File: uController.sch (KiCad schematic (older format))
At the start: 37 parts, among them J4 USB_C_Receptacle, U13 STM32F446RETx, U14 STM14_SW, Y1 16Mhz, 18pF

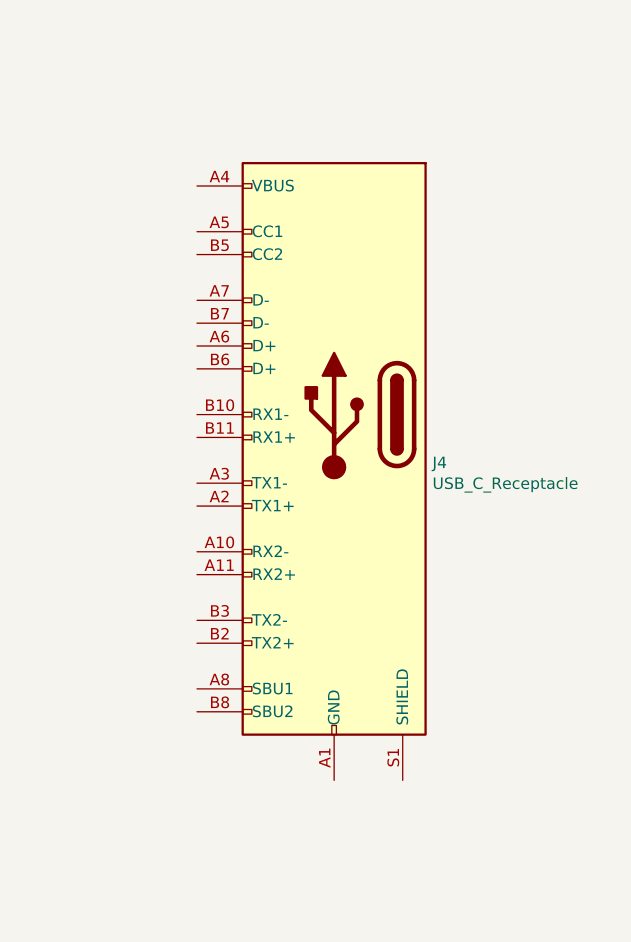
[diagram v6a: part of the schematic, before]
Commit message: USB-C PD charging and cell balancing.
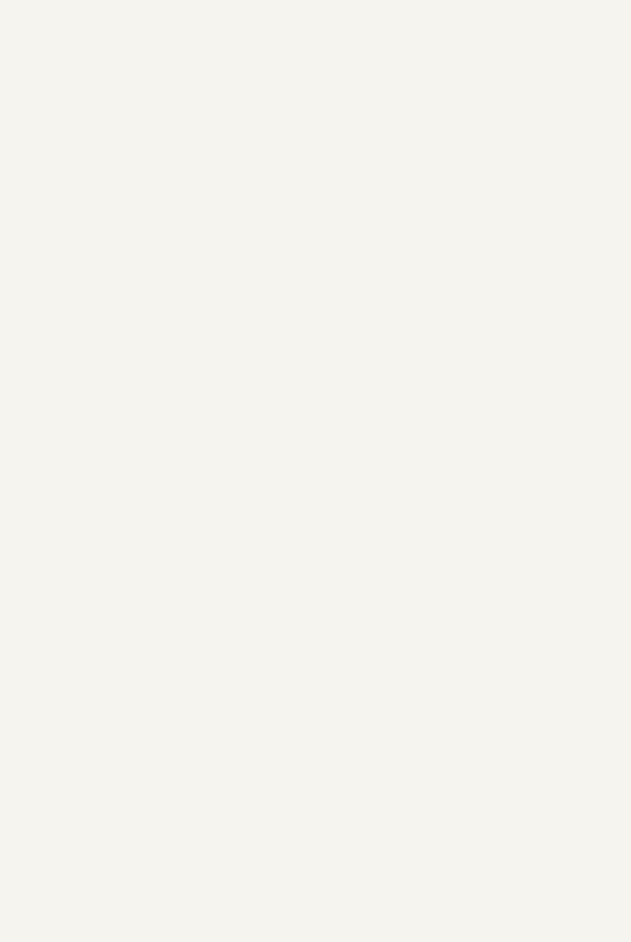
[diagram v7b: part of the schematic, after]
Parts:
- removed J4: USB_C_Receptacle, Connector_USB:USB_C_Receptacle_GCT_USB4085, symbol synermycha-electronics-rescue:USB_C_Receptacle-Connector
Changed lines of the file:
@@
 Connection ~ 3600 5750
-$Comp
-L Device:R_Small R42
-U 1 1 5E839F84
-P 2700 3550
-F 0 "R42" H 2759 3596 50  0000 L CNN
-F 1 "140R" H 2759 3505 50  0000 L CNN
-F 2 "Resistor_SMD:R_0402_1005Metric" H 2700 3550 50  0001 C CNN
-F 3 "~" H 2700 3550 50  0001 C CNN
-	1    2700 3550
-	1    0    0    1
-$EndComp
 $Comp
 L Device:R_Small R43
@@
 F 3 "~" H 3600 5850 50  0001 C CNN
 	1    3600 5850
-	-1   0    0    1
-$EndComp
-$Comp
-L Device:LED_Small D16
-U 1 1 5E8A288C
-P 2700 3750
-F 0 "D16" V 2750 3550 50  0000 L CNN
-F 1 "YELLOW" V 2650 3400 50  0000 L CNN
-F 2 "LED_SMD:LED_0402_1005Metric" V 2700 3750 50  0001 C CNN
-F 3 "~" V 2700 3750 50  0001 C CNN
-	1    2700 3750
-	0    -1   -1   0
-$EndComp
-$Comp
-L Device:R_Small R50
-U 1 1 5E8A7FAC
-P 2400 5650
-F 0 "R50" H 2341 5604 50  0000 R CNN
-F 1 "140R" H 2341 5695 50  0000 R CNN
-F 2 "Resistor_SMD:R_0402_1005Metric" H 2400 5650 50  0001 C CNN
-F 3 "~" H 2400 5650 50  0001 C CNN
-	1    2400 5650
 	-1   0    0    1
 $EndComp
@@
 Connection ~ 7150 4650
 $Comp
+L power:+3V3 #PWR0137
+U 1 1 5F64C720
+P 4000 5550
+F 0 "#PWR0137" H 4000 5400 50  0001 C CNN
+F 1 "+3V3" H 4015 5723 50  0000 C CNN
+F 2 "" H 4000 5550 50  0001 C CNN
+F 3 "" H 4000 5550 50  0001 C CNN
+	1    4000 5550
+	1    0    0    -1
+$EndComp
+$Comp
+L power:+3V3 #PWR0140
+U 1 1 5F64D886
+P 3100 3250
+F 0 "#PWR0140" H 3100 3100 50  0001 C CNN
+F 1 "+3V3" H 3115 3423 50  0000 C CNN
+F 2 "" H 3100 3250 50  0001 C CNN
+F 3 "" H 3100 3250 50  0001 C CNN
+	1    3100 3250
+	1    0    0    -1
+$EndComp
+$Comp
+L power:+3V3 #PWR0141
+U 1 1 5F64E077
+P 3100 3900
+F 0 "#PWR0141" H 3100 3750 50  0001 C CNN
+F 1 "+3V3" H 3115 4073 50  0000 C CNN
+F 2 "" H 3100 3900 50  0001 C CNN
+F 3 "" H 3100 3900 50  0001 C CNN
+	1    3100 3900
+	1    0    0    -1
+$EndComp
+$Comp
+L power:+3V3 #PWR0142
+U 1 1 5F657B9E
+P 7300 1650
+F 0 "#PWR0142" H 7300 1500 50  0001 C CNN
+F 1 "+3V3" H 7315 1823 50  0000 C CNN
+F 2 "" H 7300 1650 50  0001 C CNN
+F 3 "" H 7300 1650 50  0001 C CNN
+	1    7300 1650
+	1    0    0    -1
+$EndComp
+Wire Wire Line
+	2650 4100 2700 4100
+Connection ~ 2700 4100
+Wire Wire Line
+	2700 4100 3100 4100
+Wire Wire Line
+	2650 3450 2700 3450
+Connection ~ 2700 3450
+Wire Wire Line
+	2700 3450 3100 3450
+$Comp
+L power:GND #PWR0139
+U 1 1 5F7F8216
+P 7850 2250
+F 0 "#PWR0139" H 7850 2000 50  0001 C CNN
+F 1 "GND" H 7855 2077 50  0000 C CNN
+F 2 "" H 7850 2250 50  0001 C CNN
+F 3 "" H 7850 2250 50  0001 C CNN
+	1    7850 2250
+	1    0    0    -1
+$EndComp
+$Comp
+L power:GND #PWR0143
+U 1 1 5F7FF6EF
+P 3600 6150
+F 0 "#PWR0143" H 3600 5900 50  0001 C CNN
+F 1 "GND" H 3605 5977 50  0000 C CNN
+F 2 "" H 3600 6150 50  0001 C CNN
+F 3 "" H 3600 6150 50  0001 C CNN
+	1    3600 6150
+	1    0    0    -1
+$EndComp
+$Comp
+L power:GND #PWR0135
+U 1 1 5F7F5F84
+P 2400 5950
+F 0 "#PWR0135" H 2400 5700 50  0001 C CNN
+F 1 "GND" H 2405 5777 50  0000 C CNN
+F 2 "" H 2400 5950 50  0001 C CNN
+F 3 "" H 2400 5950 50  0001 C CNN
+	1    2400 5950
+	1    0    0    -1
+$EndComp
+$Comp
+L power:GND #PWR0136
+U 1 1 5F7F697D
+P 2700 4500
+F 0 "#PWR0136" H 2700 4250 50  0001 C CNN
+F 1 "GND" H 2705 4327 50  0000 C CNN
+F 2 "" H 2700 4500 50  0001 C CNN
+F 3 "" H 2700 4500 50  0001 C CNN
+	1    2700 4500
+	1    0    0    -1
+$EndComp
+$Comp
+L power:GND #PWR0138
+U 1 1 5F7F738B
+P 2700 3850
+F 0 "#PWR0138" H 2700 3600 50  0001 C CNN
+F 1 "GND" H 2705 3677 50  0000 C CNN
+F 2 "" H 2700 3850 50  0001 C CNN
+F 3 "" H 2700 3850 50  0001 C CNN
+	1    2700 3850
+	1    0    0    -1
+$EndComp
+$Comp
+L Device:R_Small R42
+U 1 1 5E839F84
+P 2700 3550
+F 0 "R42" H 2759 3596 50  0000 L CNN
+F 1 "140R" H 2759 3505 50  0000 L CNN
+F 2 "Resistor_SMD:R_0402_1005Metric" H 2700 3550 50  0001 C CNN
+F 3 "~" H 2700 3550 50  0001 C CNN
+	1    2700 3550
+	1    0    0    1
+$EndComp
+$Comp
+L Device:LED_Small D16
+U 1 1 5E8A288C
+P 2700 3750
+F 0 "D16" V 2750 3550 50  0000 L CNN
+F 1 "YELLOW" V 2650 3400 50  0000 L CNN
+F 2 "LED_SMD:LED_0402_1005Metric" V 2700 3750 50  0001 C CNN
+F 3 "~" V 2700 3750 50  0001 C CNN
+	1    2700 3750
+	0    -1   -1   0
+$EndComp
+$Comp
 L power:+3V3 #PWR0134
 U 1 1 5F64A100
@@
 $EndComp
 $Comp
-L power:+3V3 #PWR0137
-U 1 1 5F64C720
-P 4000 5550
-F 0 "#PWR0137" H 4000 5400 50  0001 C CNN
-F 1 "+3V3" H 4015 5723 50  0000 C CNN
-F 2 "" H 4000 5550 50  0001 C CNN
-F 3 "" H 4000 5550 50  0001 C CNN
-	1    4000 5550
-	1    0    0    -1
-$EndComp
-$Comp
-L power:+3V3 #PWR0140
-U 1 1 5F64D886
-P 3100 3250
-F 0 "#PWR0140" H 3100 3100 50  0001 C CNN
-F 1 "+3V3" H 3115 3423 50  0000 C CNN
-F 2 "" H 3100 3250 50  0001 C CNN
-F 3 "" H 3100 3250 50  0001 C CNN
-	1    3100 3250
-	1    0    0    -1
-$EndComp
-$Comp
-L power:+3V3 #PWR0141
-U 1 1 5F64E077
-P 3100 3900
-F 0 "#PWR0141" H 3100 3750 50  0001 C CNN
-F 1 "+3V3" H 3115 4073 50  0000 C CNN
-F 2 "" H 3100 3900 50  0001 C CNN
-F 3 "" H 3100 3900 50  0001 C CNN
-	1    3100 3900
-	1    0    0    -1
-$EndComp
-$Comp
-L power:+3V3 #PWR0142
-U 1 1 5F657B9E
-P 7300 1650
-F 0 "#PWR0142" H 7300 1500 50  0001 C CNN
-F 1 "+3V3" H 7315 1823 50  0000 C CNN
-F 2 "" H 7300 1650 50  0001 C CNN
-F 3 "" H 7300 1650 50  0001 C CNN
-	1    7300 1650
-	1    0    0    -1
-$EndComp
-$Comp
-L synermycha-electronics-rescue:USB_C_Receptacle-Connector J4
-U 1 1 5F661DD8
-P 10200 3100
-AR Path="/5F661DD8" Ref="J4"  Part="1"
-AR Path="/5E5F551F/5F661DD8" Ref="J4"  Part="1"
-F 0 "J4" H 9770 2889 50  0000 R CNN
-F 1 "USB_C_Receptacle" H 9770 2798 50  0000 R CNN
-F 2 "Connector_USB:USB_C_Receptacle_GCT_USB4085" H 10350 3100 50  0001 C CNN
-F 3 "https://www.usb.org/sites/default/files/documents/usb_type-c.zip" H 10350 3100 50  0001 C CNN
-	1    10200 3100
-	-1   0    0    -1
+L Device:R_Small R50
+U 1 1 5E8A7FAC
+P 2400 5650
+F 0 "R50" H 2341 5604 50  0000 R CNN
+F 1 "140R" H 2341 5695 50  0000 R CNN
+F 2 "Resistor_SMD:R_0402_1005Metric" H 2400 5650 50  0001 C CNN
+F 3 "~" H 2400 5650 50  0001 C CNN
+	1    2400 5650
+	-1   0    0    1
 $EndComp
 $Comp
@@
 	0    1    -1   0
 $EndComp
-Wire Wire Line
-	2650 4100 2700 4100
-Connection ~ 2700 4100
-Wire Wire Line
-	2700 4100 3100 4100
-Wire Wire Line
-	2650 3450 2700 3450
-Connection ~ 2700 3450
-Wire Wire Line
-	2700 3450 3100 3450
-$Comp
-L power:GND #PWR0135
-U 1 1 5F7F5F84
-P 2400 5950
-F 0 "#PWR0135" H 2400 5700 50  0001 C CNN
-F 1 "GND" H 2405 5777 50  0000 C CNN
-F 2 "" H 2400 5950 50  0001 C CNN
-F 3 "" H 2400 5950 50  0001 C CNN
-	1    2400 5950
-	1    0    0    -1
-$EndComp
-$Comp
-L power:GND #PWR0136
-U 1 1 5F7F697D
-P 2700 4500
-F 0 "#PWR0136" H 2700 4250 50  0001 C CNN
-F 1 "GND" H 2705 4327 50  0000 C CNN
-F 2 "" H 2700 4500 50  0001 C CNN
-F 3 "" H 2700 4500 50  0001 C CNN
-	1    2700 4500
-	1    0    0    -1
-$EndComp
-$Comp
-L power:GND #PWR0138
-U 1 1 5F7F738B
-P 2700 3850
-F 0 "#PWR0138" H 2700 3600 50  0001 C CNN
-F 1 "GND" H 2705 3677 50  0000 C CNN
-F 2 "" H 2700 3850 50  0001 C CNN
-F 3 "" H 2700 3850 50  0001 C CNN
-	1    2700 3850
-	1    0    0    -1
-$EndComp
-$Comp
-L power:GND #PWR0139
-U 1 1 5F7F8216
-P 7850 2250
-F 0 "#PWR0139" H 7850 2000 50  0001 C CNN
-F 1 "GND" H 7855 2077 50  0000 C CNN
-F 2 "" H 7850 2250 50  0001 C CNN
-F 3 "" H 7850 2250 50  0001 C CNN
-	1    7850 2250
-	1    0    0    -1
-$EndComp
-$Comp
-L power:GND #PWR0143
-U 1 1 5F7FF6EF
-P 3600 6150
-F 0 "#PWR0143" H 3600 5900 50  0001 C CNN
-F 1 "GND" H 3605 5977 50  0000 C CNN
-F 2 "" H 3600 6150 50  0001 C CNN
-F 3 "" H 3600 6150 50  0001 C CNN
-	1    3600 6150
-	1    0    0    -1
-$EndComp
 $EndSCHEMATC

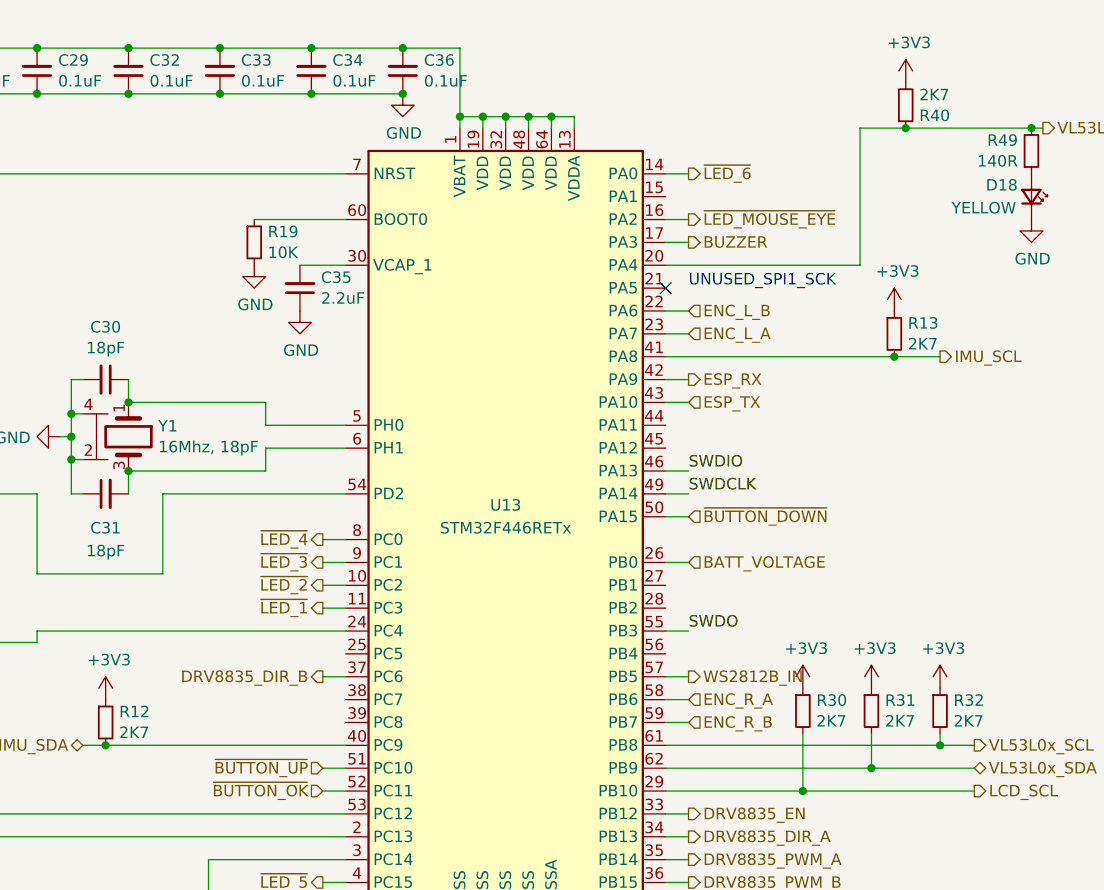
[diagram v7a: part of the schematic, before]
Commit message: Updated BT module connection, 3D models and wiring.
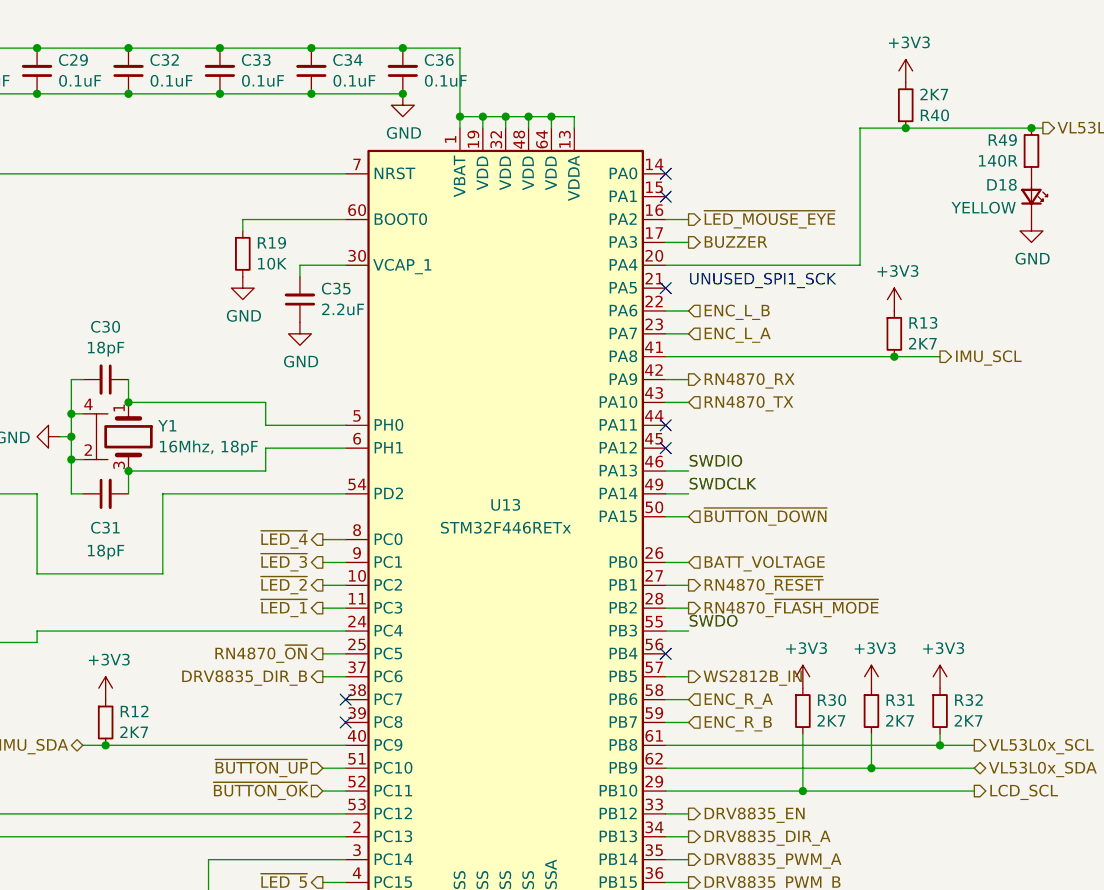
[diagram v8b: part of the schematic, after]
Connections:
- net RN4870_~ON: now reaches U13.25 (PC5)
- net RN4870_~RESET: now reaches U13.27 (PB1)
- net RN4870_~FLASH_MODE: now reaches U13.28 (PB2)
- net ESP_RX renamed RN4870_RX
- net ESP_TX renamed RN4870_TX
- net ~LED_6: no longer names the net of U13.14 (PA0)
- no-connect marks 2 -> 9
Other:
- moved on the sheet: C35, R19
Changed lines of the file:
@@
 $Descr A4 11693 8268
 encoding utf-8
-Sheet 10 11
+Sheet 8 11
 Title ""
 Date ""
@@
 Comment4 ""
 $EndDescr
-$Comp
-L MCU_ST_STM32F4:STM32F446RETx U13
-U 1 1 5E5FC006
-P 5550 3550
-F 0 "U13" H 5550 3600 50  0000 C CNN
-F 1 "STM32F446RETx" H 5550 3500 50  0000 C CNN
-F 2 "Package_QFP:LQFP-64_10x10mm_P0.5mm" H 4950 1850 50  0001 R CNN
-F 3 "http://www.st.com/st-web-ui/static/active/en/resource/technical/document/datasheet/DM00141306.pdf" H 5550 3550 50  0001 C CNN
-	1    5550 3550
-	1    0    0    -1
-$EndComp
 Wire Wire Line
 	3900 3350 4500 3350
@@
 IMU_SCL
 Text HLabel 6350 2950 2    50   Output ~ 0
-ESP_RX
+RN4870_RX
 Text HLabel 6350 3050 2    50   Input ~ 0
-ESP_TX
+RN4870_TX
 Text HLabel 6350 3750 2    50   Input ~ 0
 BATT_VOLTAGE
@@
 L Device:C_Small C35
 U 1 1 5E630928
-P 4650 2550
-F 0 "C35" H 4558 2504 50  0000 R CNN
-F 1 "2.2uF" H 4558 2595 50  0000 R CNN
-F 2 "Capacitor_SMD:C_0603_1608Metric" H 4650 2550 50  0001 C CNN
-F 3 "~" H 4650 2550 50  0001 C CNN
-	1    4650 2550
+P 4650 2600
+F 0 "C35" H 4558 2554 50  0000 R CNN
+F 1 "2.2uF" H 4558 2645 50  0000 R CNN
+F 2 "Capacitor_SMD:C_0603_1608Metric" H 4650 2600 50  0001 C CNN
+F 3 "~" H 4650 2600 50  0001 C CNN
+	1    4650 2600
 	-1   0    0    1
 $EndComp
@@
 L Device:R_Small R19
 U 1 1 5E6321B0
-P 4450 2350
-F 0 "R19" H 4509 2396 50  0000 L CNN
-F 1 "10K" H 4509 2305 50  0000 L CNN
-F 2 "Resistor_SMD:R_0402_1005Metric" H 4450 2350 50  0001 C CNN
-F 3 "~" H 4450 2350 50  0001 C CNN
-	1    4450 2350
+P 4400 2400
+F 0 "R19" H 4459 2446 50  0000 L CNN
+F 1 "10K" H 4459 2355 50  0000 L CNN
+F 2 "Resistor_SMD:R_0402_1005Metric" H 4400 2400 50  0001 C CNN
+F 3 "~" H 4400 2400 50  0001 C CNN
+	1    4400 2400
 	1    0    0    -1
 $EndComp
@@
 L power:GND #PWR0149
 U 1 1 5E633AFC
-P 4450 2450
-F 0 "#PWR0149" H 4450 2200 50  0001 C CNN
-F 1 "GND" H 4455 2277 50  0000 C CNN
-F 2 "" H 4450 2450 50  0001 C CNN
-F 3 "" H 4450 2450 50  0001 C CNN
-	1    4450 2450
+P 4400 2500
+F 0 "#PWR0149" H 4400 2250 50  0001 C CNN
+F 1 "GND" H 4405 2327 50  0000 C CNN
+F 2 "" H 4400 2500 50  0001 C CNN
+F 3 "" H 4400 2500 50  0001 C CNN
+	1    4400 2500
 	1    0    0    -1
 $EndComp
@@
 L power:GND #PWR0150
 U 1 1 5E6343F0
-P 4650 2650
-F 0 "#PWR0150" H 4650 2400 50  0001 C CNN
-F 1 "GND" H 4655 2477 50  0000 C CNN
-F 2 "" H 4650 2650 50  0001 C CNN
-F 3 "" H 4650 2650 50  0001 C CNN
-	1    4650 2650
+P 4650 2700
+F 0 "#PWR0150" H 4650 2450 50  0001 C CNN
+F 1 "GND" H 4655 2527 50  0000 C CNN
+F 2 "" H 4650 2700 50  0001 C CNN
+F 3 "" H 4650 2700 50  0001 C CNN
+	1    4650 2700
 	1    0    0    -1
 $EndComp
 Wire Wire Line
 	4850 2450 4650 2450
-Wire Wire Line
-	4850 2250 4450 2250
 Wire Wire Line
 	5350 1850 5350 1800
@@
 Wire Wire Line
 	4750 3950 4850 3950
-Text HLabel 6350 2050 2    50   Output ~ 0
-~LED_6
-Wire Wire Line
-	6350 2050 6250 2050
 Text HLabel 6350 4250 2    50   Output ~ 0
 WS2812B_IN
@@
 	0    1    -1   0
 $EndComp
+NoConn ~ 6250 3150
+NoConn ~ 6250 3250
+NoConn ~ 6250 2150
+NoConn ~ 6250 2050
+Wire Wire Line
+	4650 2500 4650 2450
+Wire Wire Line
+	4400 2250 4400 2300
+Wire Wire Line
+	4400 2250 4850 2250
+NoConn ~ 6250 4150
+NoConn ~ 4850 4350
+NoConn ~ 4850 4450
+Text HLabel 4750 4150 0    50   Output ~ 0
+RN4870_~ON
+Text HLabel 6350 3850 2    50   Output ~ 0
+RN4870_~RESET
+Text HLabel 6350 3950 2    50   Output ~ 0
+RN4870_~FLASH_MODE
+Wire Wire Line
+	4750 4150 4850 4150
+$Comp
+L MCU_ST_STM32F4:STM32F446RETx U13
+U 1 1 5E5FC006
+P 5550 3550
+F 0 "U13" H 5550 3600 50  0000 C CNN
+F 1 "STM32F446RETx" H 5550 3500 50  0000 C CNN
+F 2 "Package_QFP:LQFP-64_10x10mm_P0.5mm" H 4950 1850 50  0001 R CNN
+F 3 "http://www.st.com/st-web-ui/static/active/en/resource/technical/document/datasheet/DM00141306.pdf" H 5550 3550 50  0001 C CNN
+	1    5550 3550
+	1    0    0    -1
+$EndComp
+Wire Wire Line
+	6350 3850 6250 3850
+Wire Wire Line
+	6250 3950 6350 3950
 $EndSCHEMATC
